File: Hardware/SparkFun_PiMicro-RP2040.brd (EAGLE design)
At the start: 17.8 x 33 mm, 105 parts, among them J2 Qwiic, J5 USB Female Type C Connector, U1 3.3V, U2 RP2040, U3 WS2812-2020, U4 W25QXX128MBIT, Y1 12MHz

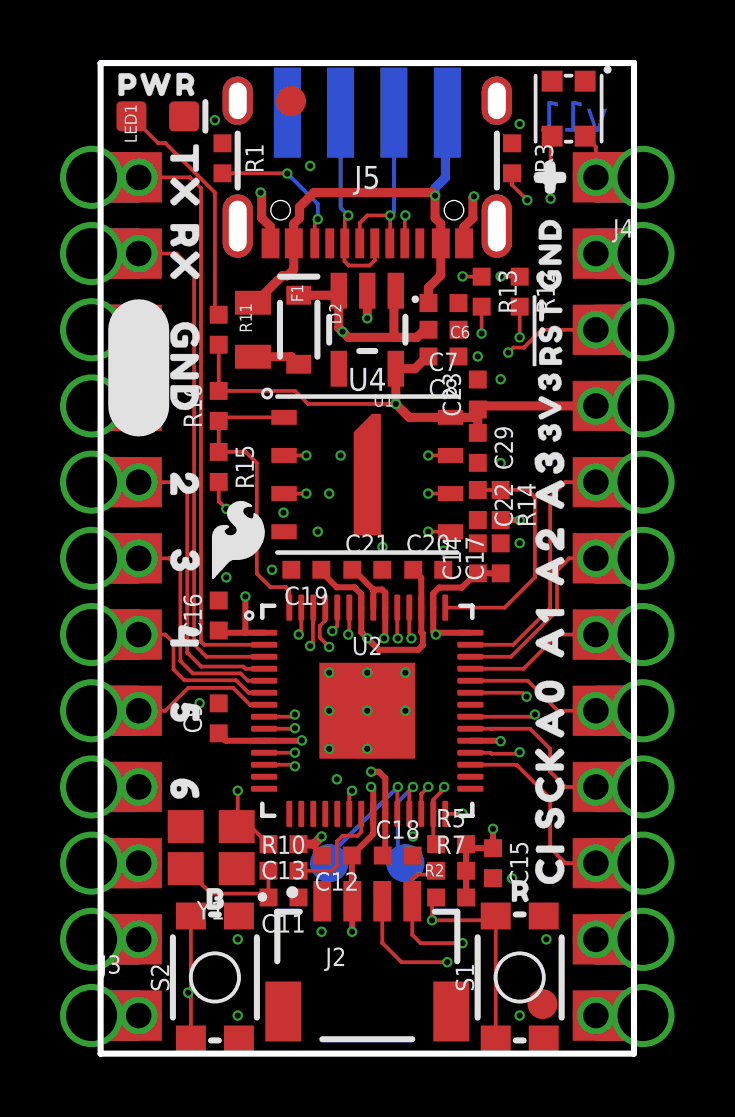
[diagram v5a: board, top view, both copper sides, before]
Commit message: Add DO TP for WS2812
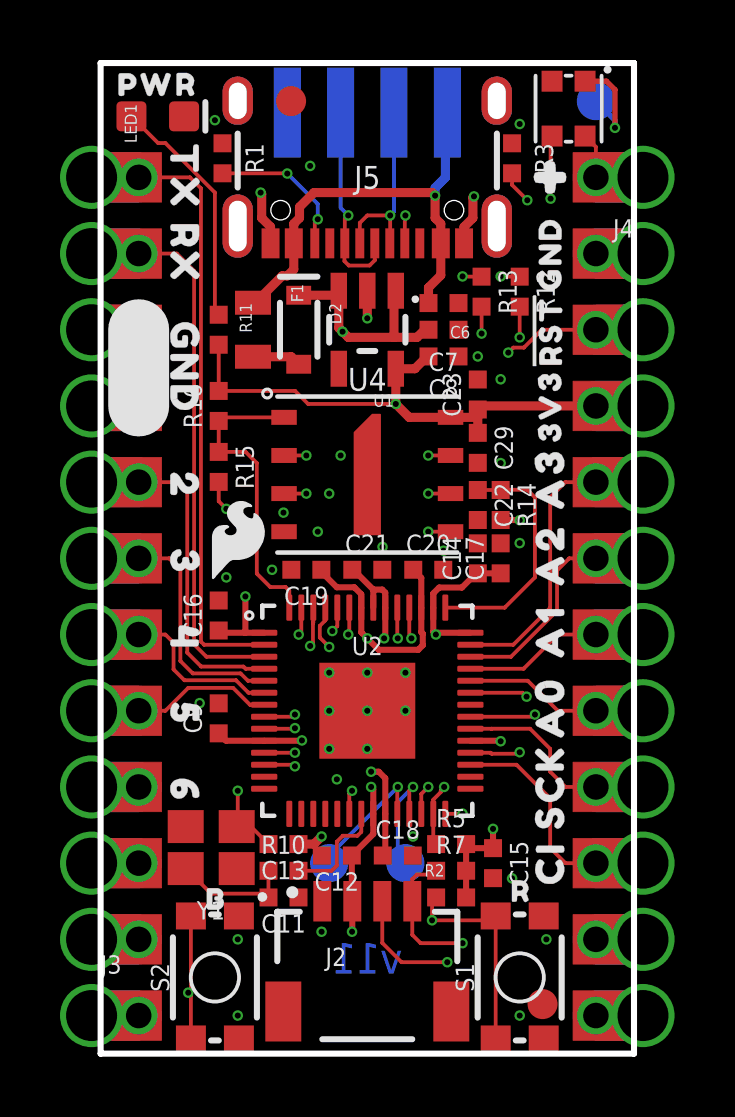
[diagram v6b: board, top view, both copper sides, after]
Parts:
- added TP3: (no value), SparkFun-Connectors:PAD.03X.05
- added U$18: (no value), output:C0
- added U$35: (no value), output:D1
- added U$40: (no value), output:DO0
- moved U$3 0.57 mm to (1.52, 31.5)
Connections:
- new net N$1: TP3.P$1, U3.1
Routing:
- net N$1: track 0.00 -> 3.53 mm, vias 0 -> 1
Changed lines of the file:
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@@
 <wire x1="17.78" y1="0" x2="17.78" y2="33.02" width="0.2032" layer="20"/>
 <wire x1="17.78" y1="33.02" x2="0" y2="33.02" width="0.2032" layer="20"/>
-<text x="15.748" y="31.242" size="1.016" layer="16" font="vector" ratio="25" rot="MR0" align="center">v11</text>
+<text x="8.89" y="3.175" size="1.016" layer="16" font="vector" ratio="25" rot="MR0" align="center">v11</text>
 <wire x1="1.27" y1="24.13" x2="1.27" y2="21.59" width="2.032" layer="21"/>
 <wire x1="1.27" y1="24.13" x2="1.27" y2="21.59" width="2.032" layer="22"/>
@@
 <attribute name="VALUE" value="10k" x="11.188696875" y="5.791196875" size="0.4064" layer="27"/>
 </element>
-<element name="U$3" library="SparkFun-Aesthetics" package="OSHW-LOGO-MINI" value="OSHW-LOGOMINI" x="2.032" y="31.242" smashed="yes" rot="MR0"/>
+<element name="U$3" library="SparkFun-Aesthetics" package="OSHW-LOGO-MINI" value="OSHW-LOGOMINI" x="1.524" y="31.496" smashed="yes" rot="MR0"/>
 <element name="C6" library="SparkFun-Capacitors" package="0402-TIGHT" value="1.0uF" x="11.43" y="25.019" smashed="yes" rot="R180">
 <attribute name="NAME" x="12.319003125" y="24.257" size="0.4064" layer="25" font="vector" rot="R180"/>
@@
 <element name="U$4" library="output" package="PRO_MICRO0" value="" x="9.398" y="14.478" smashed="yes" rot="MR270"/>
 <element name="U$38" library="output" package="RP20401" value="" x="11.43" y="14.351" smashed="yes" rot="MR270"/>
+<element name="U$18" library="output" package="C0" value="" x="7.493" y="4.953" smashed="yes" rot="MR0"/>
+<element name="U$35" library="output" package="D1" value="" x="10.033" y="4.953" smashed="yes" rot="MR0"/>
+<element name="TP3" library="SparkFun-Connectors" package="PAD.03X.05" value="" x="16.51" y="31.75" smashed="yes" rot="MR0"/>
+<element name="U$40" library="output" package="DO0" value="" x="14.986" y="31.623" smashed="yes" rot="MR270"/>
 </elements>
 <signals>
@@
 <via x="8.89" y="12.7" extent="1-16" drill="0.2"/>
 <contactref element="U3" pad="2"/>
-<wire x1="16.51" y1="26.67" x2="18.08" y2="26.67" width="0" layer="19" extent="1-1"/>
-<wire x1="12.115" y1="27.01" x2="16.51" y2="26.67" width="0" layer="19" extent="1-1"/>
-<wire x1="11.93" y1="25.019" x2="12.115" y2="27.01" width="0" layer="19" extent="1-1"/>
-<wire x1="11.93" y1="24.13" x2="11.93" y2="25.019" width="0" layer="19" extent="1-1"/>
-<wire x1="11.93" y1="23.241" x2="11.93" y2="24.13" width="0" layer="19" extent="1-1"/>
-<wire x1="12.573" y1="23.241" x2="11.93" y2="23.241" width="0" layer="19" extent="1-1"/>
-<wire x1="12.573" y1="22.471" x2="12.573" y2="23.241" width="0" layer="19" extent="1-1"/>
-<wire x1="13.335" y1="22.479" x2="12.573" y2="22.471" width="0" layer="19" extent="1-1"/>
-<wire x1="13.716" y1="30.345" x2="12.446" y2="28.575" width="0" layer="19" extent="1-1"/>
-<wire x1="13.97" y1="30.988" x2="13.716" y2="30.345" width="0" layer="19" extent="1-1"/>
-<wire x1="15.05" y1="32.415" x2="13.97" y2="30.988" width="0" layer="19" extent="1-1"/>
-<wire x1="12.573" y1="19.693" x2="12.573" y2="22.471" width="0" layer="19" extent="1-1"/>
-<wire x1="13.335" y1="19.685" x2="12.573" y2="19.693" width="0" layer="19" extent="1-1"/>
-<wire x1="12.573" y1="17.788" x2="12.573" y2="19.693" width="0" layer="19" extent="1-1"/>
-<wire x1="12.573" y1="17.01" x2="12.573" y2="17.788" width="0" layer="19" extent="1-1"/>
-<wire x1="13.335" y1="17.01" x2="12.573" y2="17.01" width="0" layer="19" extent="1-1"/>
-<wire x1="13.97" y1="17.018" x2="13.335" y2="17.01" width="0" layer="19" extent="1-1"/>
-<wire x1="11.43" y1="16.764" x2="12.573" y2="17.01" width="0" layer="19" extent="1-1"/>
-<wire x1="11.422" y1="16.129" x2="11.43" y2="16.764" width="0" layer="19" extent="1-1"/>
-<wire x1="9.39" y1="16.129" x2="11.422" y2="16.129" width="0" layer="19" extent="1-1"/>
-<wire x1="9.398" y1="16.891" x2="9.39" y2="16.129" width="0" layer="19" extent="1-1"/>
-<wire x1="6.358" y1="16.129" x2="9.39" y2="16.129" width="0" layer="19" extent="1-1"/>
-<wire x1="5.715" y1="16.129" x2="6.358" y2="16.129" width="0" layer="19" extent="1-1"/>
-<wire x1="6.115" y1="17.399" x2="6.358" y2="16.129" width="0" layer="19" extent="1-1"/>
-<wire x1="6.096" y1="18.034" x2="6.115" y2="17.399" width="0" layer="19" extent="1-1"/>
-<wire x1="4.191" y1="15.875" x2="5.715" y2="16.129" width="0" layer="19" extent="1-1"/>
-<wire x1="3.937" y1="15.105" x2="4.191" y2="15.875" width="0" layer="19" extent="1-1"/>
-<wire x1="8.89" y1="25.4301" x2="11.93" y2="25.019" width="0" layer="19" extent="1-1"/>
-<wire x1="3.937" y1="11.676" x2="3.937" y2="15.105" width="0" layer="19" extent="1-1"/>
-<wire x1="3.302" y1="11.684" x2="3.937" y2="11.676" width="0" layer="19" extent="1-1"/>
-<wire x1="8.89" y1="12.7" x2="9.39" y2="16.129" width="0" layer="19" extent="1-1"/>
-<wire x1="10.16" y1="12.7" x2="8.89" y2="12.7" width="0" layer="19" extent="1-1"/>
-<wire x1="7.62" y1="12.7" x2="8.89" y2="12.7" width="0" layer="19" extent="1-1"/>
-<wire x1="10.16" y1="11.43" x2="10.16" y2="12.7" width="0" layer="19" extent="1-1"/>
-<wire x1="8.89" y1="11.43" x2="8.89" y2="12.7" width="0" layer="19" extent="1-1"/>
-<wire x1="8.89" y1="10.16" x2="8.89" y2="11.43" width="0" layer="19" extent="1-1"/>
-<wire x1="7.62" y1="10.16" x2="8.89" y2="10.16" width="0" layer="19" extent="1-1"/>
-<wire x1="7.874" y1="9.144" x2="7.62" y2="10.16" width="0" layer="19" extent="1-1"/>
-<wire x1="7.89" y1="7.9935" x2="7.874" y2="9.144" width="0" layer="19" extent="1-1"/>
-<wire x1="7.366" y1="7.239" x2="7.89" y2="7.9935" width="0" layer="19" extent="1-1"/>
-<wire x1="7.374" y1="6.604" x2="7.366" y2="7.239" width="0" layer="19" extent="1-1"/>
-<wire x1="7.62" y1="11.43" x2="7.62" y2="12.7" width="0" layer="19" extent="1-1"/>
-<wire x1="7.39" y1="5.08" x2="7.374" y2="6.604" width="0" layer="19" extent="1-1"/>
-<wire x1="6.596" y1="5.207" x2="7.39" y2="5.08" width="0" layer="19" extent="1-1"/>
-<wire x1="7.366" y1="4.064" x2="7.39" y2="5.08" width="0" layer="19" extent="1-1"/>
-<wire x1="4.61" y1="4.59" x2="6.596" y2="5.207" width="0" layer="19" extent="1-1"/>
-<wire x1="4.572" y1="3.81" x2="4.61" y2="4.59" width="0" layer="19" extent="1-1"/>
-<wire x1="4.572" y1="1.27" x2="4.572" y2="3.81" width="0" layer="19" extent="1-1"/>
-<wire x1="4.61" y1="0.49" x2="4.572" y2="1.27" width="0" layer="19" extent="1-1"/>
-<wire x1="10.414" y1="7.239" x2="7.89" y2="7.9935" width="0" layer="19" extent="1-1"/>
-<wire x1="10.406" y1="6.604" x2="10.414" y2="7.239" width="0" layer="19" extent="1-1"/>
-<wire x1="13.081" y1="5.85" x2="10.406" y2="6.604" width="0" layer="19" extent="1-1"/>
-<wire x1="13.716" y1="5.842" x2="13.081" y2="5.85" width="0" layer="19" extent="1-1"/>
-<wire x1="14.77" y1="4.59" x2="13.716" y2="5.842" width="0" layer="19" extent="1-1"/>
-<wire x1="14.859" y1="3.81" x2="14.77" y2="4.59" width="0" layer="19" extent="1-1"/>
-<wire x1="13.97" y1="1.27" x2="14.859" y2="3.81" width="0" layer="19" extent="1-1"/>
-<wire x1="14.77" y1="0.49" x2="13.97" y2="1.27" width="0" layer="19" extent="1-1"/>
-<wire x1="5.665" y1="27.01" x2="8.89" y2="25.4301" width="0" layer="19" extent="1-1"/>
-<wire x1="6.985" y1="29.591" x2="5.334" y2="28.702" width="0" layer="19" extent="1-1"/>
-<wire x1="6.223" y1="31.369" x2="6.985" y2="29.591" width="0" layer="19" extent="16-16"/>
-<wire x1="4.064" y1="30.345" x2="5.334" y2="28.702" width="0" layer="19" extent="1-1"/>
-<wire x1="3.81" y1="31.115" x2="4.064" y2="30.345" width="0" layer="19" extent="1-1"/>
-<wire x1="2.782" y1="31.242" x2="3.81" y2="31.115" width="0" layer="19" extent="1-1"/>
-<wire x1="1.27" y1="24.13" x2="5.665" y2="27.01" width="0" layer="19" extent="1-1"/>
-<wire x1="-0.3" y1="24.13" x2="1.27" y2="24.13" width="0" layer="19" extent="1-1"/>
-<wire x1="1.27" y1="21.59" x2="1.27" y2="24.13" width="0" layer="19" extent="1-1"/>
-<wire x1="-0.3" y1="21.59" x2="1.27" y2="21.59" width="0" layer="19" extent="1-1"/>
 </signal>
 <signal name="N$38">
@@
 <wire x1="9.84" y1="22.8299" x2="9.84" y2="21.656" width="0.3048" layer="1"/>
 <via x="9.84" y="21.656" extent="1-16" drill="0.2"/>
-<wire x1="13.335" y1="16.01" x2="13.335" y2="17.788" width="0" layer="19" extent="1-1"/>
-<wire x1="9.49" y1="14.8665" x2="11.09" y2="14.8665" width="0" layer="19" extent="1-1"/>
-<wire x1="12.573" y1="20.693" x2="13.335" y2="17.788" width="0" layer="19" extent="1-1"/>
-<wire x1="12.3265" y1="10.43" x2="12.3265" y2="14.03" width="0" layer="19" extent="1-1"/>
-<wire x1="13.081" y1="7.493" x2="13.335" y2="10.414" width="0" layer="19" extent="1-1"/>
-<wire x1="9.09" y1="7.9935" x2="12.184" y2="6.985" width="0" layer="19" extent="1-1"/>
-<wire x1="6.71105625" y1="10.441" x2="9.017" y2="8.89" width="0" layer="19" extent="1-1"/>
-<wire x1="3.937" y1="14.105" x2="3.937" y2="10.676" width="0" layer="19" extent="1-1"/>
 </signal>
 <signal name="!RESET!">
@@
 <wire x1="15" y1="30.535" x2="15.05" y2="30.585" width="0.127" layer="1"/>
 </signal>
+<signal name="N$1">
+<contactref element="U3" pad="1"/>
+<contactref element="TP3" pad="P$1"/>
+<wire x1="16.51" y1="31.75" x2="17.145" y2="31.115" width="0.1778" layer="16"/>
+<wire x1="17.145" y1="31.115" x2="17.145" y2="30.861" width="0.1778" layer="16"/>
+<via x="17.145" y="30.861" extent="1-16" drill="0.2"/>
+<wire x1="17.145" y1="30.861" x2="17.145" y2="32.131" width="0.1778" layer="1"/>
+<wire x1="16.861" y1="32.415" x2="16.15" y2="32.415" width="0.1778" layer="1"/>
+<wire x1="17.145" y1="32.131" x2="16.861" y2="32.415" width="0.1778" layer="1"/>
+</signal>
 </signals>
